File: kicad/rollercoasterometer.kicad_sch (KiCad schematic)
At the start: 12 parts, among them J120 STANDOFF, J125 STANDOFF, J127 STANDOFF, J129 STANDOFF, U104 Teensy4.1

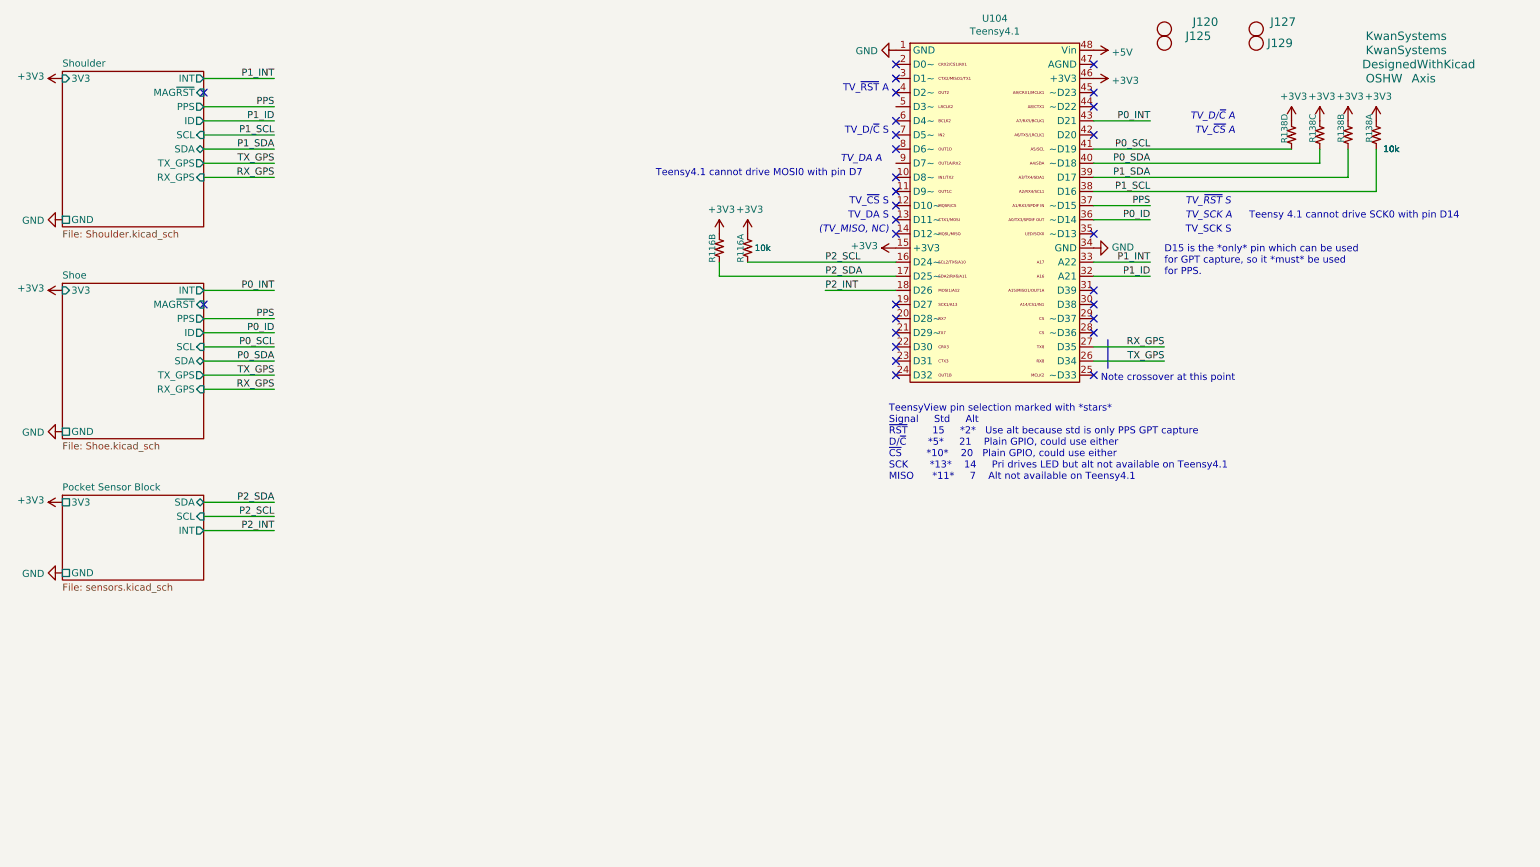
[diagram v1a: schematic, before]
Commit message: One shining moment
Commit board while it still works
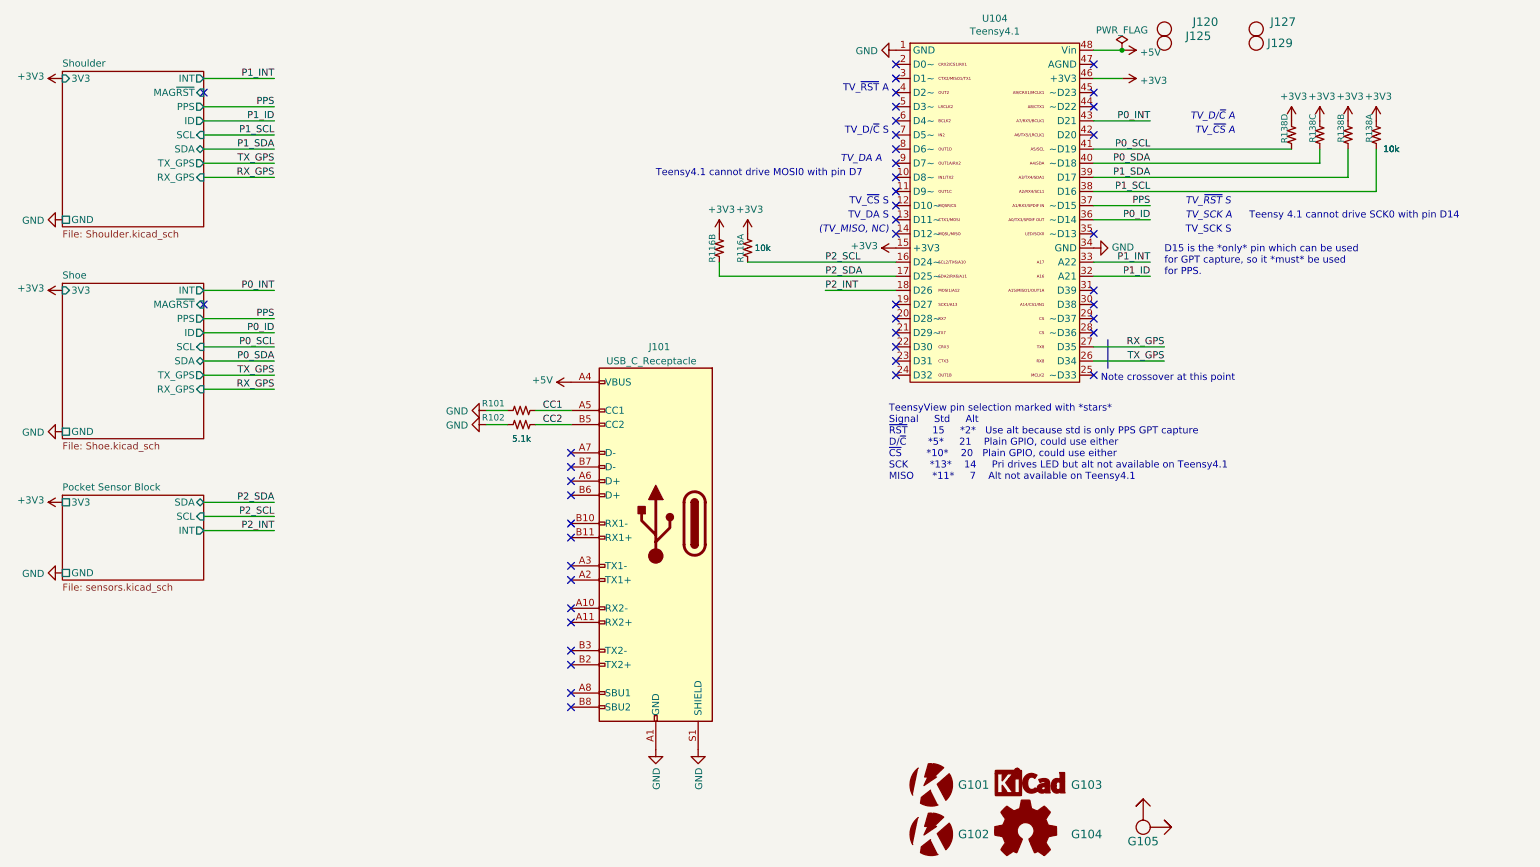
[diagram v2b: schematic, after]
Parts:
- added J101: USB_C_Receptacle, KwanSystems:USB_C_Amphenol_MidMount, symbol Connector:USB_C_Receptacle
- added R101, R102: 5.1k, Resistor_SMD:R_0402_1005Metric, symbol KwanSystems:RESISTOR
- G105: symbol KwanSystems:OSHW -> KwanSystems:Axis
- R116: Digikey (none) -> 742C043103JPCT-ND; Purpose (none) -> I2C bus pullup
- R138: Digikey (none) -> 741C083103JPCT-ND; Purpose (none) -> I2C bus pullup
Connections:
- net +5V: now also J101.A4 (VBUS), J101.A9 (VBUS), J101.B4 (VBUS), J101.B9 (VBUS)
- net GND: now also J101.A1 (GND), J101.A12 (GND), J101.B1 (GND), J101.B12 (GND), J101.S1 (SHIELD), R101.1, R102.1
- new net CC1: J101.A5 (CC1), R101.2
- new net CC2: J101.B5 (CC2), R102.2
- no-connect marks 29 -> 45

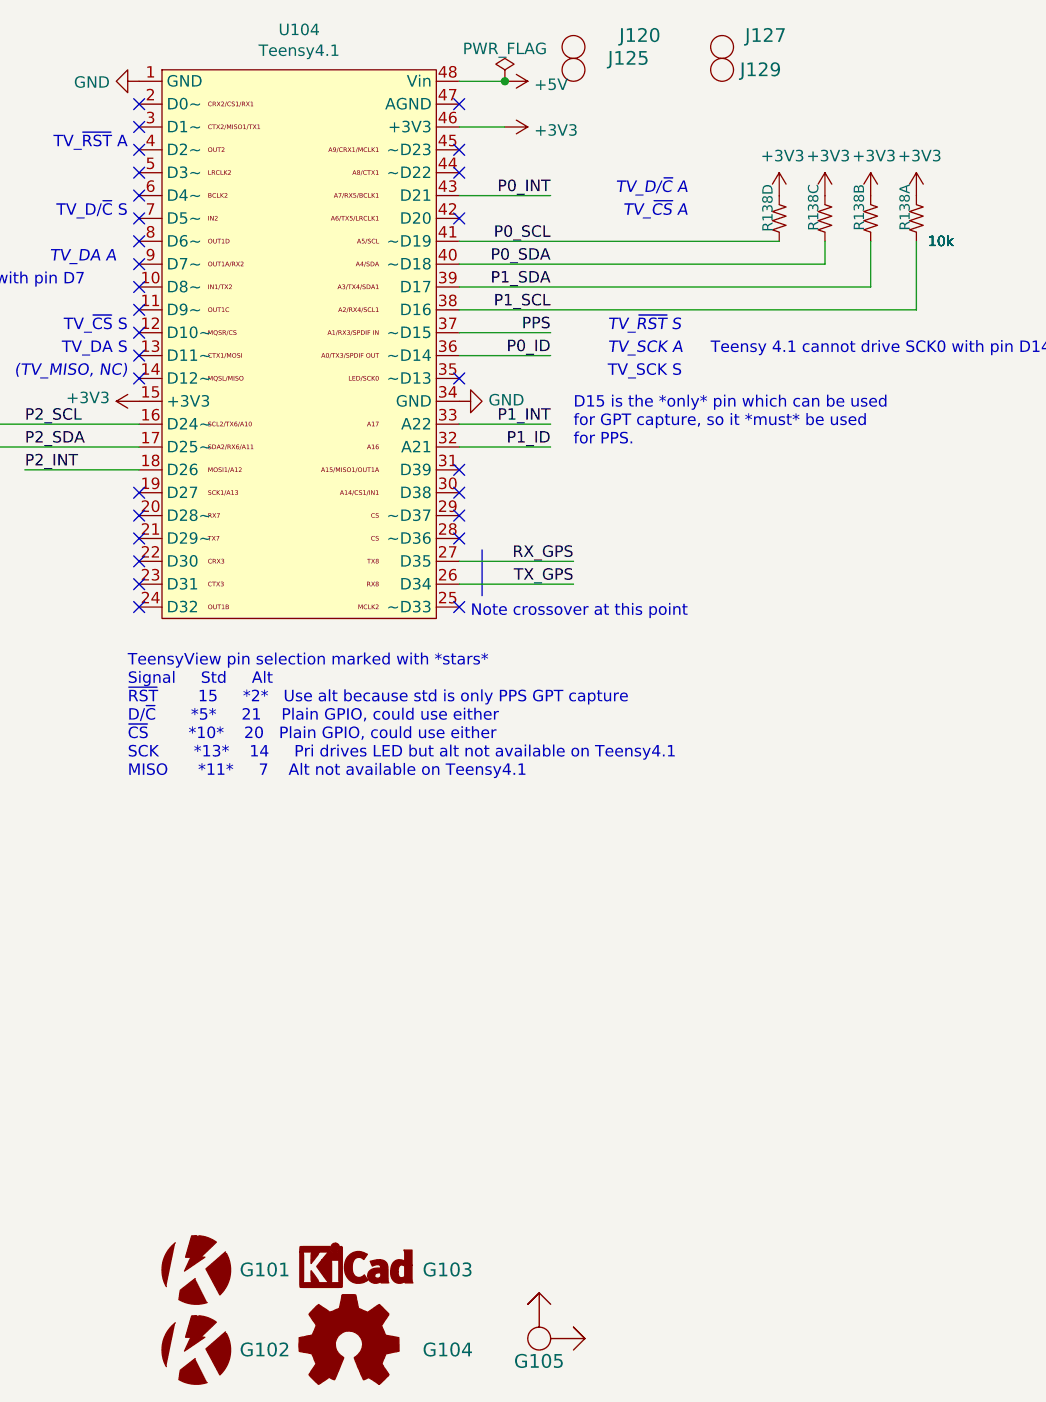
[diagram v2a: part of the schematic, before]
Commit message: Updated graphical symbols
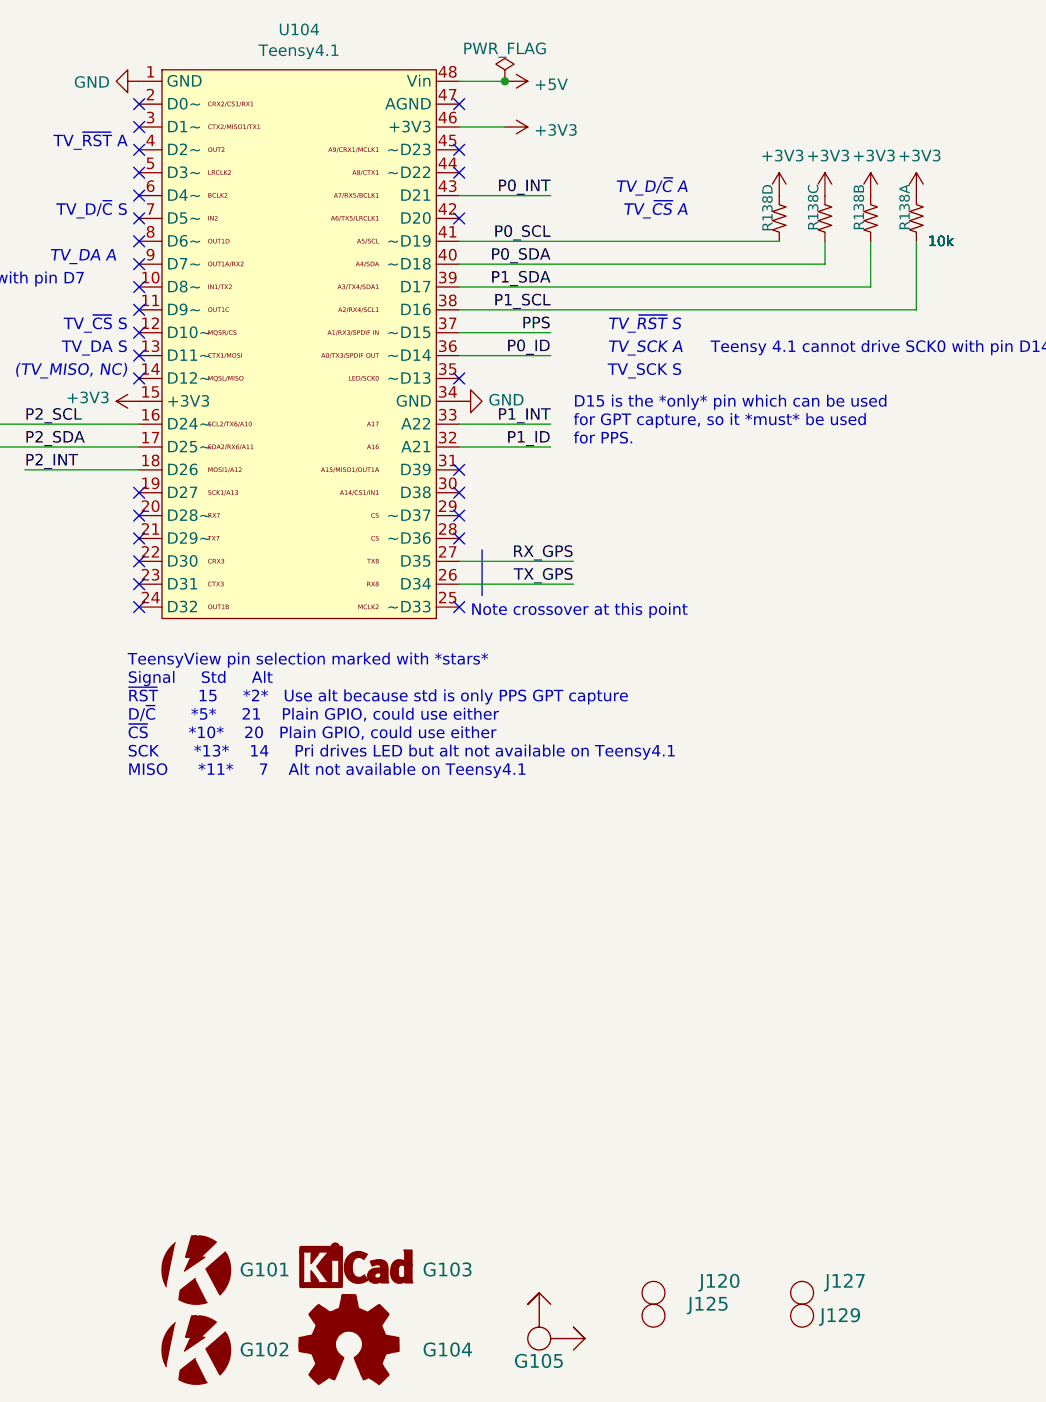
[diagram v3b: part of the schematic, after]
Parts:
- G101, G102, G103, G104, G105, J120, J125, J127, J129: now left out of the parts list
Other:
- moved on the sheet: J120, J125, J127, J129
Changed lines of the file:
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@@
   )
   (symbol (lib_id "KwanSystems:DesignedWithKicad") (at 199.39 153.67 0) (unit 1)
-    (in_bom yes) (on_board yes)
+    (in_bom no) (on_board yes)
     (property "Reference" "G103" (id 0) (at 209.55 152.4 0)
       (effects (font (size 1.524 1.524)))
@@
     )
   )
-  (symbol (lib_id "KwanSystems:STANDOFF") (at 240.03 16.51 0) (unit 1)
-    (in_bom yes) (on_board yes)
-    (property "Reference" "J127" (id 0) (at 242.57 15.24 0)
+  (symbol (lib_name "STANDOFF_1") (lib_id "KwanSystems:STANDOFF") (at 248.92 154.94 0) (unit 1)
+    (in_bom no) (on_board yes)
+    (property "Reference" "J127" (id 0) (at 251.46 153.67 0)
       (effects (font (size 1.524 1.524)) (justify left))
     )
-    (property "Value" "STANDOFF" (id 1) (at 242.0112 17.8562 0)
-      (effects (font (size 1.524 1.524)) (justify left) hide)
-    )
-    (property "Footprint" "KwanSystems:STANDOFF_NONPLATED" (id 2) (at 240.03 16.51 0)
-      (effects (font (size 1.524 1.524)) hide)
-    )
-    (property "Datasheet" "" (id 3) (at 240.03 16.51 0)
+    (property "Value" "STANDOFF" (id 1) (at 250.9012 156.2862 0)
+      (effects (font (size 1.524 1.524)) (justify left) hide)
+    )
+    (property "Footprint" "KwanSystems:STANDOFF_NONPLATED" (id 2) (at 248.92 154.94 0)
+      (effects (font (size 1.524 1.524)) hide)
+    )
+    (property "Datasheet" "" (id 3) (at 248.92 154.94 0)
       (effects (font (size 1.524 1.524)) hide)
     )
@@
     (pin "1")
   )
-  (symbol (lib_name "KwanSystems_1") (lib_id "KwanSystems:KwanSystems") (at 181.61 152.4 0) (unit 1)
-    (in_bom yes) (on_board yes)
+  (symbol (lib_id "KwanSystems:KwanSystems") (at 181.61 152.4 0) (unit 1)
+    (in_bom no) (on_board yes)
     (property "Reference" "G101" (id 0) (at 189.23 152.4 0)
       (effects (font (size 1.524 1.524)))
@@
   )
   (symbol (lib_id "KwanSystems:Axis") (at 219.71 160.02 0) (unit 1)
-    (in_bom yes) (on_board yes)
+    (in_bom no) (on_board yes)
     (property "Reference" "G105" (id 0) (at 219.71 162.56 0)
       (effects (font (size 1.524 1.524)))
@@
   )
   (symbol (lib_id "KwanSystems:KwanSystems") (at 181.61 161.29 0) (unit 1)
-    (in_bom yes) (on_board yes)
+    (in_bom no) (on_board yes)
     (property "Reference" "G102" (id 0) (at 189.23 161.29 0)
       (effects (font (size 1.524 1.524)))
@@
     (pin "1")
   )
-  (symbol (lib_id "KwanSystems:STANDOFF") (at 223.52 19.05 0) (unit 1)
-    (in_bom yes) (on_board yes)
-    (property "Reference" "J125" (id 0) (at 227.33 17.78 0)
+  (symbol (lib_name "STANDOFF_2") (lib_id "KwanSystems:STANDOFF") (at 232.41 157.48 0) (unit 1)
+    (in_bom no) (on_board yes)
+    (property "Reference" "J125" (id 0) (at 236.22 156.21 0)
       (effects (font (size 1.524 1.524)) (justify left))
     )
-    (property "Value" "STANDOFF" (id 1) (at 225.5012 20.3962 0)
-      (effects (font (size 1.524 1.524)) (justify left) hide)
-    )
-    (property "Footprint" "KwanSystems:STANDOFF_NONPLATED" (id 2) (at 223.52 19.05 0)
-      (effects (font (size 1.524 1.524)) hide)
-    )
-    (property "Datasheet" "" (id 3) (at 223.52 19.05 0)
+    (property "Value" "STANDOFF" (id 1) (at 234.3912 158.8262 0)
+      (effects (font (size 1.524 1.524)) (justify left) hide)
+    )
+    (property "Footprint" "KwanSystems:STANDOFF_NONPLATED" (id 2) (at 232.41 157.48 0)
+      (effects (font (size 1.524 1.524)) hide)
+    )
+    (property "Datasheet" "" (id 3) (at 232.41 157.48 0)
       (effects (font (size 1.524 1.524)) hide)
     )
@@
     (pin "6")
   )
-  (symbol (lib_name "OSHW_1") (lib_id "KwanSystems:OSHW") (at 198.12 161.29 0) (unit 1)
-    (in_bom yes) (on_board yes)
+  (symbol (lib_id "KwanSystems:OSHW") (at 198.12 161.29 0) (unit 1)
+    (in_bom no) (on_board yes)
     (property "Reference" "G104" (id 0) (at 209.55 161.29 0)
       (effects (font (size 1.524 1.524)))
@@
     (pin "1")
   )
-  (symbol (lib_id "KwanSystems:STANDOFF") (at 223.52 16.51 0) (unit 1)
-    (in_bom yes) (on_board yes)
-    (property "Reference" "J120" (id 0) (at 228.6 15.24 0)
+  (symbol (lib_id "KwanSystems:STANDOFF") (at 232.41 154.94 0) (unit 1)
+    (in_bom no) (on_board yes)
+    (property "Reference" "J120" (id 0) (at 237.49 153.67 0)
       (effects (font (size 1.524 1.524)) (justify left))
     )
-    (property "Value" "STANDOFF" (id 1) (at 225.5012 17.8562 0)
-      (effects (font (size 1.524 1.524)) (justify left) hide)
-    )
-    (property "Footprint" "KwanSystems:STANDOFF_NONPLATED" (id 2) (at 223.52 16.51 0)
-      (effects (font (size 1.524 1.524)) hide)
-    )
-    (property "Datasheet" "" (id 3) (at 223.52 16.51 0)
+    (property "Value" "STANDOFF" (id 1) (at 234.3912 156.2862 0)
+      (effects (font (size 1.524 1.524)) (justify left) hide)
+    )
+    (property "Footprint" "KwanSystems:STANDOFF_NONPLATED" (id 2) (at 232.41 154.94 0)
+      (effects (font (size 1.524 1.524)) hide)
+    )
+    (property "Datasheet" "" (id 3) (at 232.41 154.94 0)
       (effects (font (size 1.524 1.524)) hide)
     )
@@
     (pin "1")
   )
-  (symbol (lib_id "KwanSystems:STANDOFF") (at 240.03 19.05 0) (unit 1)
-    (in_bom yes) (on_board yes)
-    (property "Reference" "J129" (id 0) (at 242.0112 19.05 0)
+  (symbol (lib_name "STANDOFF_3") (lib_id "KwanSystems:STANDOFF") (at 248.92 157.48 0) (unit 1)
+    (in_bom no) (on_board yes)
+    (property "Reference" "J129" (id 0) (at 250.9012 157.48 0)
       (effects (font (size 1.524 1.524)) (justify left))
     )
-    (property "Value" "STANDOFF" (id 1) (at 242.0112 20.3962 0)
-      (effects (font (size 1.524 1.524)) (justify left) hide)
-    )
-    (property "Footprint" "KwanSystems:STANDOFF_NONPLATED" (id 2) (at 240.03 19.05 0)
-      (effects (font (size 1.524 1.524)) hide)
-    )
-    (property "Datasheet" "" (id 3) (at 240.03 19.05 0)
-      (effects (font (size 1.524 1.524)) hide)
-    )
+    (property "Value" "STANDOFF" (id 1) (at 250.9012 158.8262 0)
+      (effects (font (size 1.524 1.524)) (justify left) hide)
+    )
+    (property "Footprint" "KwanSystems:STANDOFF_NONPLATED" (id 2) (at 248.92 157.48 0)
+      (effects (font (size 1.524 1.524)) hide)
+    )
+    (property "Datasheet" "" (id 3) (at 248.92 157.48 0)
+      (effects (font (size 1.524 1.524)) hide)
+    )

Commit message: Updated Digikey part numbers
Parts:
- J101: Digikey WM12856CT-ND -> 664-12402072E512ACT-ND
- R101, R102: Digikey CC marker -> P5.1KJCT-ND
- U104: Digikey 1568-DEV-16771-ND -> 1568-1527-ND
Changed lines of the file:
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@@
       (effects (font (size 1.27 1.27)) hide)
     )
-    (property "Digikey" "1568-DEV-16771-ND" (id 4) (at 193.04 50.8 0)
+    (property "Digikey" "1568-1527-ND" (id 4) (at 193.04 50.8 0)
       (effects (font (size 1.27 1.27)) hide)
     )
@@
       (effects (font (size 1.27 1.27)) hide)
     )
-    (property "Digikey" "CC marker" (id 5) (at 107.95 85.09 0)
+    (property "Digikey" "P5.1KJCT-ND" (id 5) (at 107.95 85.09 0)
       (effects (font (size 1.27 1.27)) hide)
     )
@@
       (effects (font (size 1.27 1.27)) hide)
     )
-    (property "Digikey" "WM12856CT-ND" (id 5) (at 132.08 105.41 0)
+    (property "Digikey" "664-12402072E512ACT-ND" (id 5) (at 132.08 105.41 0)
       (effects (font (size 1.27 1.27)) hide)
     )
@@
       (effects (font (size 1.27 1.27)) hide)
     )
-    (property "Digikey" "CC marker" (id 5) (at 107.95 87.63 0)
-      (effects (font (size 1.27 1.27)) hide)
-    )
+    (property "Digikey" "P5.1KJCT-ND" (id 5) (at 107.95 87.63 0)
+      (effects (font (size 1.27 1.27)) hide)
+    )
